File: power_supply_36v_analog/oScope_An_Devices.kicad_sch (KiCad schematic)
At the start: 1 part, among them J1 Conn_02x15_Odd_Even

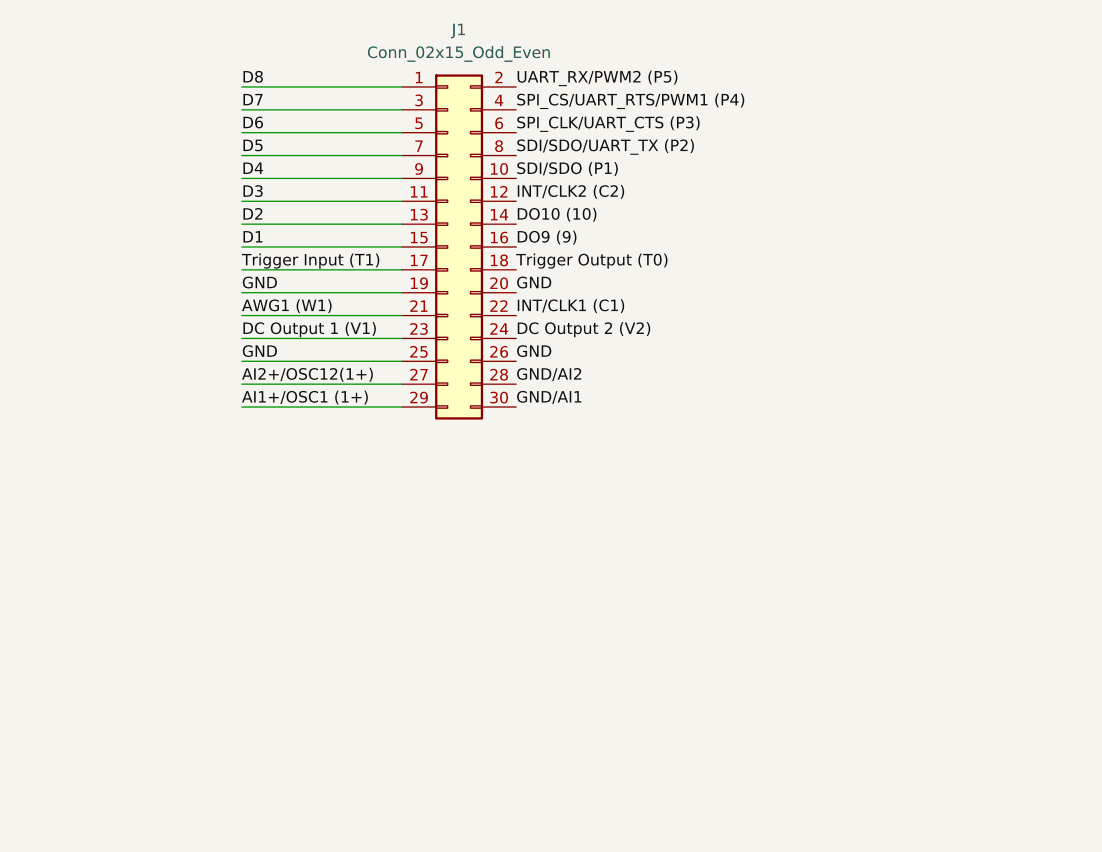
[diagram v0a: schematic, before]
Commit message: Fix pin spacing to 2.54mm like DiscoveryAnalog3 sheet
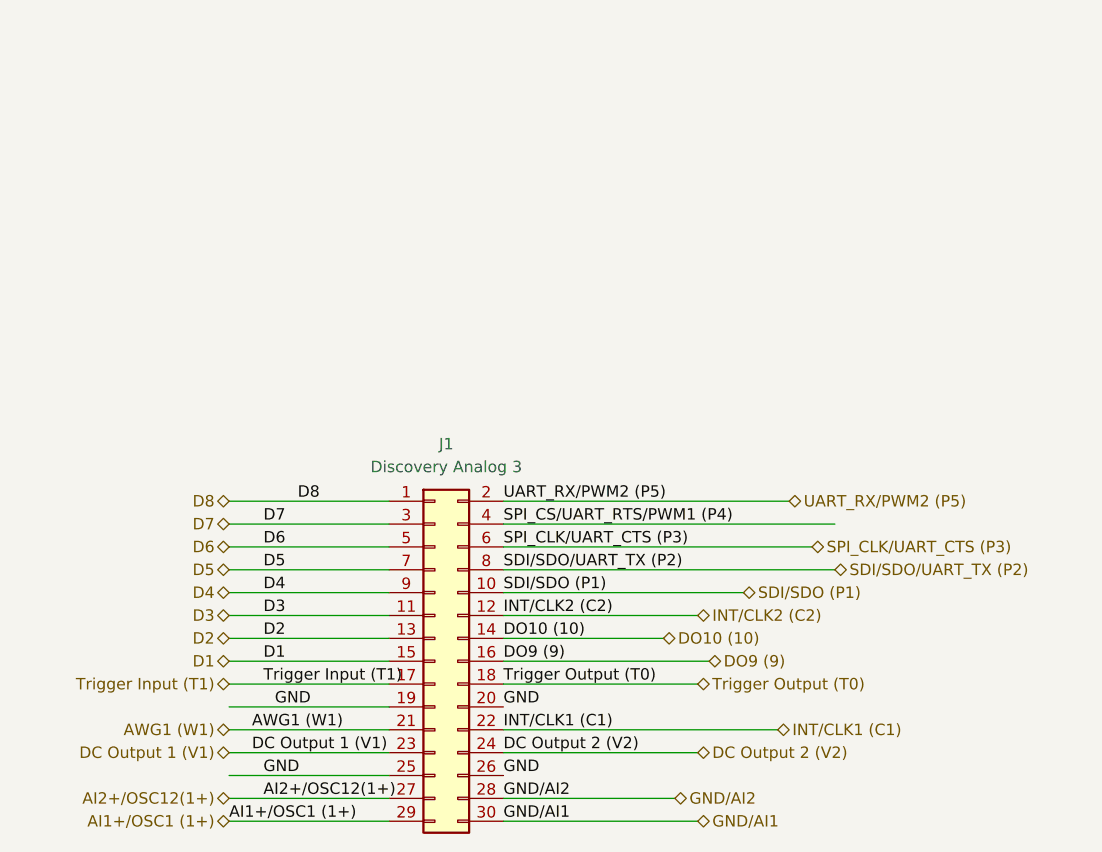
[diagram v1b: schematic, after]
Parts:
- J1: value Conn_02x15_Odd_Even -> Discovery Analog 3
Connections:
- net DC Output 2 (V2)  renamed DC Output 2 (V2)
- net DO10 (10)  renamed DO10 (10)
- net DO9 (9)  renamed DO9 (9)
- net INT/CLK1 (C1)  renamed INT/CLK1 (C1)
- net INT/CLK2 (C2)  renamed INT/CLK2 (C2)
- net SDI/SDO (P1)  renamed SDI/SDO (P1)
- net SDI/SDO/UART_TX (P2)  renamed SDI/SDO/UART_TX (P2)
- net SPI_CLK/UART_CTS (P3)  renamed SPI_CLK/UART_CTS (P3)
- net Trigger Output (T0)  renamed Trigger Output (T0)
